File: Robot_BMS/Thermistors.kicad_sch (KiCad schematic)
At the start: 6 parts

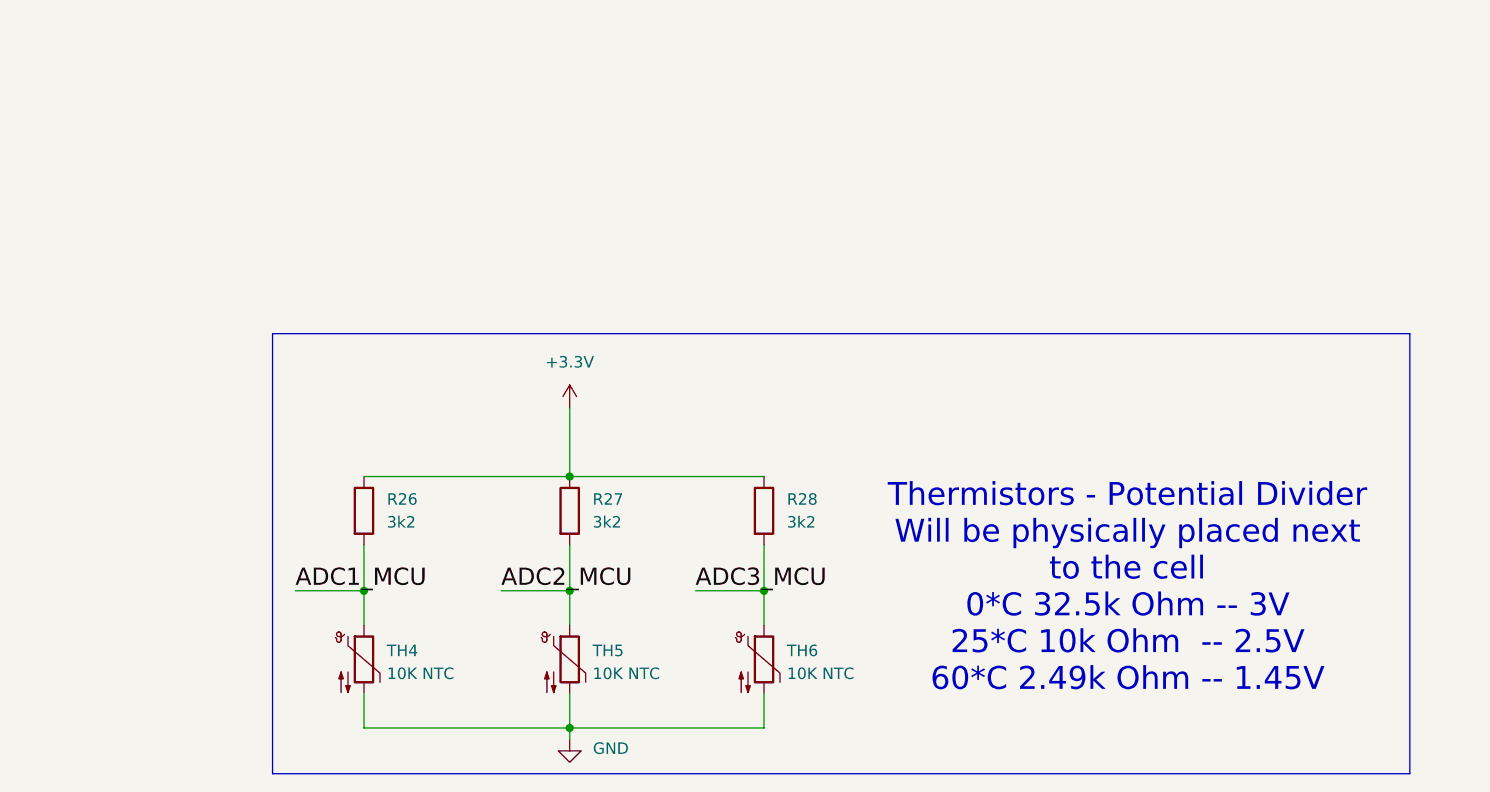
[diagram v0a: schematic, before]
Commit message: cleaning up hierarchical schematics
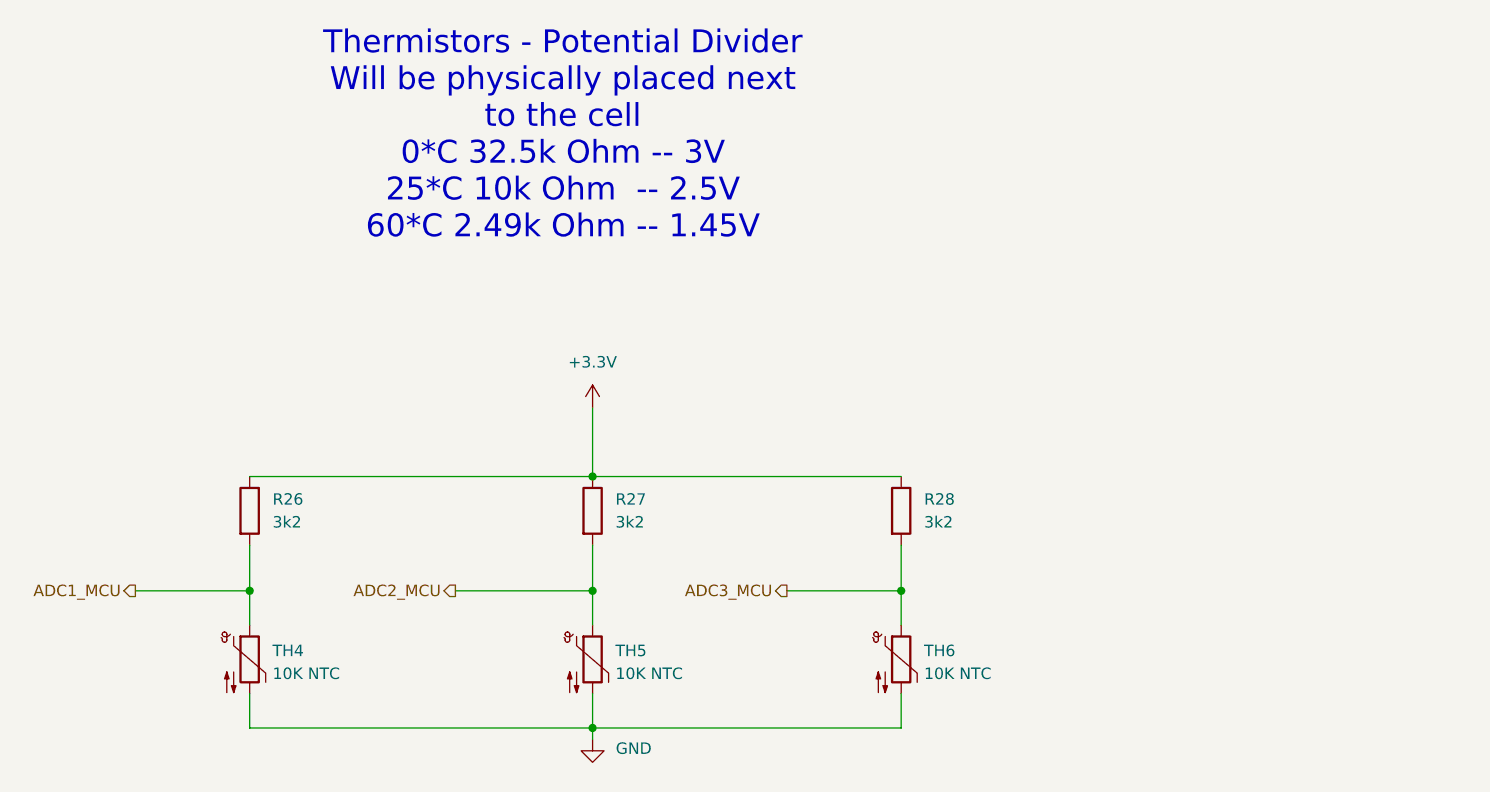
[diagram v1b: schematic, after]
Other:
- moved on the sheet: R26, R27, R28, TH4, TH5, TH6

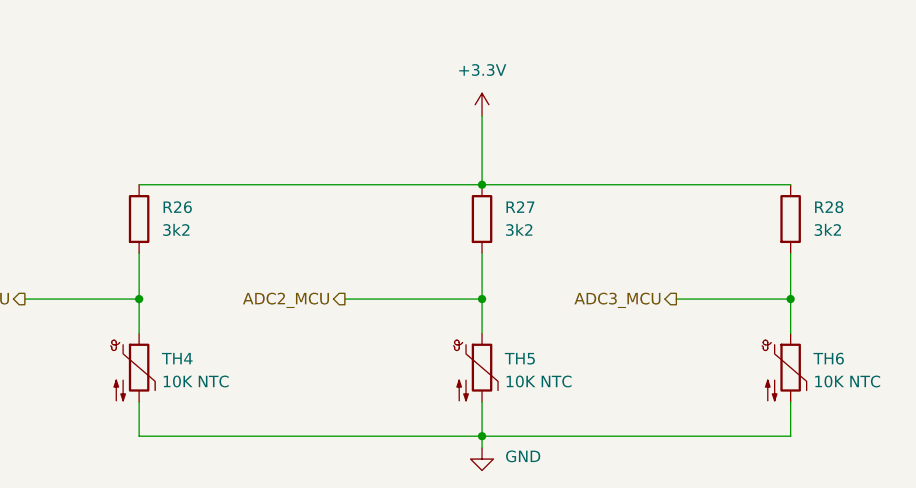
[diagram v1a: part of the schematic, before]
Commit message: DC power supply added via dc Barrel jack
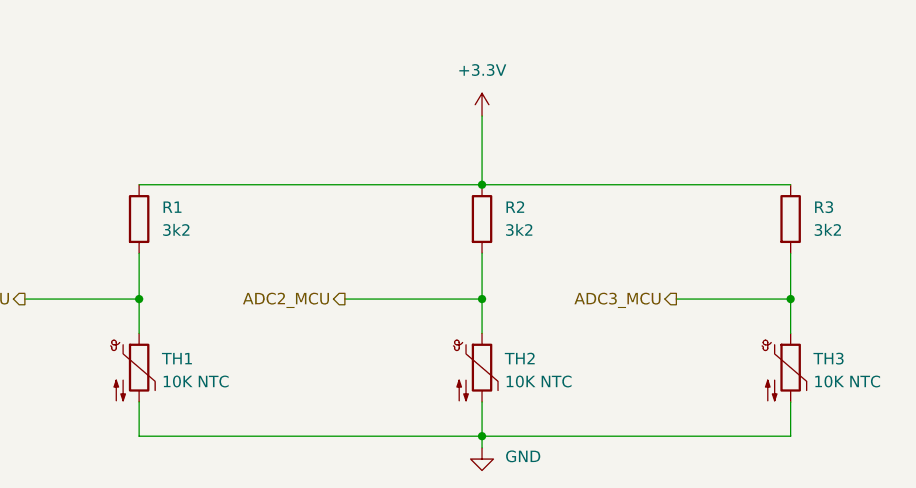
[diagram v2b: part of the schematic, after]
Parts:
- renumbered R26 to R1, R27 to R2, R28 to R3, TH4 to TH1, TH5 to TH2, TH6 to TH3
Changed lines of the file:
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@@
 		(dnp no)
 		(fields_autoplaced yes)
-		(property "Reference" "R26"
+		(property "Reference" "R1"
 			(at 96.52 101.5999 0)
 			(effects
@@
 			(project "Robot_BMS"
 				(path "/72551b1c-3d40-4199-8911-e5b015f4abec/cb04dfab-e035-4615-b482-7ed1936c63ff"
-					(reference "R26")
+					(reference "R1")
 					(unit 1)
 				)
@@
 		(dnp no)
 		(fields_autoplaced yes)
-		(property "Reference" "R28"
+		(property "Reference" "R3"
 			(at 168.91 101.5999 0)
 			(effects
@@
 			(project "Robot_BMS"
 				(path "/72551b1c-3d40-4199-8911-e5b015f4abec/cb04dfab-e035-4615-b482-7ed1936c63ff"
-					(reference "R28")
+					(reference "R3")
 					(unit 1)
 				)
@@
 		(dnp no)
 		(fields_autoplaced yes)
-		(property "Reference" "TH4"
+		(property "Reference" "TH1"
 			(at 96.52 118.4274 0)
 			(effects
@@
 			(project "Robot_BMS"
 				(path "/72551b1c-3d40-4199-8911-e5b015f4abec/cb04dfab-e035-4615-b482-7ed1936c63ff"
-					(reference "TH4")
+					(reference "TH1")
 					(unit 1)
 				)
@@
 		(dnp no)
 		(fields_autoplaced yes)
-		(property "Reference" "R27"
+		(property "Reference" "R2"
 			(at 134.62 101.5999 0)
 			(effects
@@
 			(project "Robot_BMS"
 				(path "/72551b1c-3d40-4199-8911-e5b015f4abec/cb04dfab-e035-4615-b482-7ed1936c63ff"
-					(reference "R27")
+					(reference "R2")
 					(unit 1)
 				)
@@
 		(on_board yes)
 		(dnp no)
-		(property "Reference" "#PWR010"
+		(property "Reference" "#PWR02"
 			(at 132.08 134.62 0)
 			(effects
@@
 			(project "Robot_BMS"
 				(path "/72551b1c-3d40-4199-8911-e5b015f4abec/cb04dfab-e035-4615-b482-7ed1936c63ff"
-					(reference "#PWR010")
+					(reference "#PWR02")
 					(unit 1)
 				)
@@
 		(dnp no)
 		(fields_autoplaced yes)
-		(property "Reference" "#PWR09"
+		(property "Reference" "#PWR01"
 			(at 132.08 95.25 0)
 			(effects
@@
 			(project "Robot_BMS"
 				(path "/72551b1c-3d40-4199-8911-e5b015f4abec/cb04dfab-e035-4615-b482-7ed1936c63ff"
-					(reference "#PWR09")
+					(reference "#PWR01")
 					(unit 1)
 				)
@@
 		(dnp no)
 		(fields_autoplaced yes)
-		(property "Reference" "TH6"
+		(property "Reference" "TH3"
 			(at 168.91 118.4274 0)
 			(effects
@@
 			(project "Robot_BMS"
 				(path "/72551b1c-3d40-4199-8911-e5b015f4abec/cb04dfab-e035-4615-b482-7ed1936c63ff"
-					(reference "TH6")
+					(reference "TH3")
 					(unit 1)
 				)
@@
 		(dnp no)
 		(fields_autoplaced yes)
-		(property "Reference" "TH5"
+		(property "Reference" "TH2"
 			(at 134.62 118.4274 0)
 			(effects
@@
 			(project "Robot_BMS"
 				(path "/72551b1c-3d40-4199-8911-e5b015f4abec/cb04dfab-e035-4615-b482-7ed1936c63ff"
-					(reference "TH5")
-					(unit 1)
-				)
+					(reference "TH2")
+					(unit 1)
+				)

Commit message: adding footprints and actual passive components
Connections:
- net +3.3V renamed 3V3
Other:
- note added: "All standard Passive componenets are 0603 imperial"
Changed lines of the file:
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@@
+	)
+	(junction
+		(at 137.414 91.44)
+		(diameter 0)
+		(color 0 0 0 0)
+	)
+	(junction
+		(at 132.08 91.44)
+		(diameter 0)
+		(color 0 0 0 0)
+	)
+	(junction
+		(at 132.08 128.27)
+		(diameter 0)
+		(color 0 0 0 0)
 	)
 	(junction
@@
 	(wire
 		(pts
+			(xy 137.414 91.44) (xy 139.192 91.44)
+		)
+		(stroke
+			(width 0)
+			(type default)
+		)
+	)
+	(wire
+		(pts
 			(xy 93.98 123.19) (xy 93.98 127)
 		)
@@
 		(pts
 			(xy 132.08 127) (xy 132.08 128.27)
+		)
+		(stroke
+			(width 0)
+			(type default)
+		)
+	)
+	(wire
+		(pts
+			(xy 132.08 91.44) (xy 137.414 91.44)
 		)
 		(stroke
@@
 				(size 2.54 2.54)
 			)
+		)
+	)
+	(text "All standard Passive\ncomponenets are 0603 imperial"
+		(exclude_from_sim no)
+		(at 213.868 175.768 0)
+		(effects
+			(font
+				(size 2.54 2.54)
+			)
+		)
+	)
+	(hierarchical_label "3V3"
+		(shape input)
+		(at 139.192 91.44 0)
+		(effects
+			(font
+				(size 1.27 1.27)
+			)
+			(justify left)
 		)
 	)
@@
 	)
 	(symbol
+		(lib_id "power:PWR_FLAG")
+		(at 137.414 91.44 180)
+		(unit 1)
+		(exclude_from_sim no)
+		(in_bom yes)
+		(on_board yes)
+		(dnp no)
+		(property "Reference" "#FLG02"
+			(at 137.414 93.345 0)
+			(effects
+				(font
+					(size 1.27 1.27)
+				)
+				(hide yes)
+			)
+		)
+		(property "Value" "PWR_FLAG"
+			(at 137.414 96.52 0)
+			(effects
+				(font
+					(size 1.27 1.27)
+				)
+			)
+		)
+		(property "Footprint" ""
+			(at 137.414 91.44 0)
+			(effects
+				(font
+					(size 1.27 1.27)
+				)
+				(hide yes)
+			)
+		)
+		(property "Datasheet" "~"
+			(at 137.414 91.44 0)
+			(effects
+				(font
+					(size 1.27 1.27)
+				)
+				(hide yes)
+			)
+		)
+		(property "Description" "Special symbol for telling ERC where power comes from"
+			(at 137.414 91.44 0)
+			(effects
+				(font
+					(size 1.27 1.27)
+				)
+				(hide yes)
+			)
+		)
+		(pin "1"
+		)
+		(instances
+			(project "Robot_BMS"
+				(path "/72551b1c-3d40-4199-8911-e5b015f4abec/cb04dfab-e035-4615-b482-7ed1936c63ff"
+					(reference "#FLG02")
+					(unit 1)
+				)
+			)
+		)
+	)
+	(symbol
 		(lib_id "Device:R")
 		(at 166.37 102.87 0)
@@
 	)
 	(symbol
+		(lib_id "power:PWR_FLAG")
+		(at 132.08 128.27 90)
+		(unit 1)
+		(exclude_from_sim no)
+		(in_bom yes)
+		(on_board yes)
+		(dnp no)
+		(property "Reference" "#FLG01"
+			(at 130.175 128.27 0)
+			(effects
+				(font
+					(size 1.27 1.27)
+				)
+				(hide yes)
+			)
+		)
+		(property "Value" "PWR_FLAG"
+			(at 123.444 128.524 90)
+			(effects
+				(font
+					(size 1.27 1.27)
+				)
+			)
+		)
+		(property "Footprint" ""
+			(at 132.08 128.27 0)
+			(effects
+				(font
+					(size 1.27 1.27)
+				)
+				(hide yes)
+			)
+		)
+		(property "Datasheet" "~"
+			(at 132.08 128.27 0)
+			(effects
+				(font
+					(size 1.27 1.27)
+				)
+				(hide yes)
+			)
+		)
+		(property "Description" "Special symbol for telling ERC where power comes from"
+			(at 132.08 128.27 0)
+			(effects
+				(font
+					(size 1.27 1.27)
+				)
+				(hide yes)
+			)
+		)
+		(pin "1"
+		)
+		(instances
+			(project "Robot_BMS"
+				(path "/72551b1c-3d40-4199-8911-e5b015f4abec/cb04dfab-e035-4615-b482-7ed1936c63ff"
+					(reference "#FLG01")
+					(unit 1)
+				)
+			)
+		)
+	)
+	(symbol
 		(lib_id "power:GND")
 		(at 132.08 128.27 0)
@@
 			)
 		)
-		(property "Value" "+3.3V"
+		(property "Value" "3V3"
 			(at 132.08 86.36 0)
 			(effects

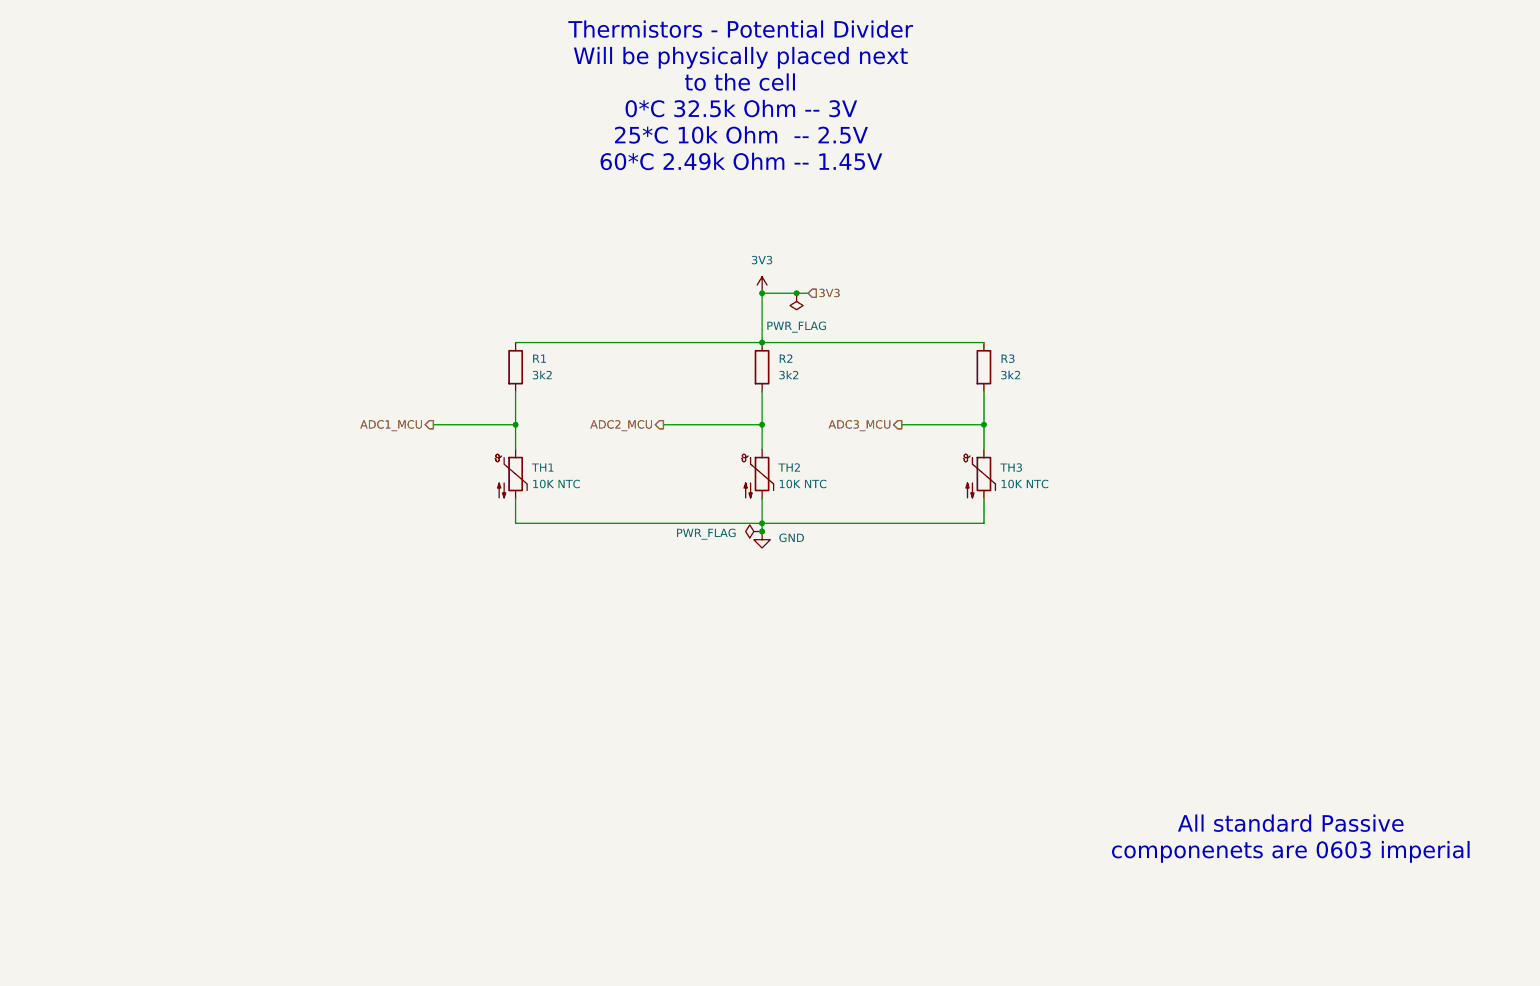
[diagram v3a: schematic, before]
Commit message: adding footprints and actual passive components pt.2
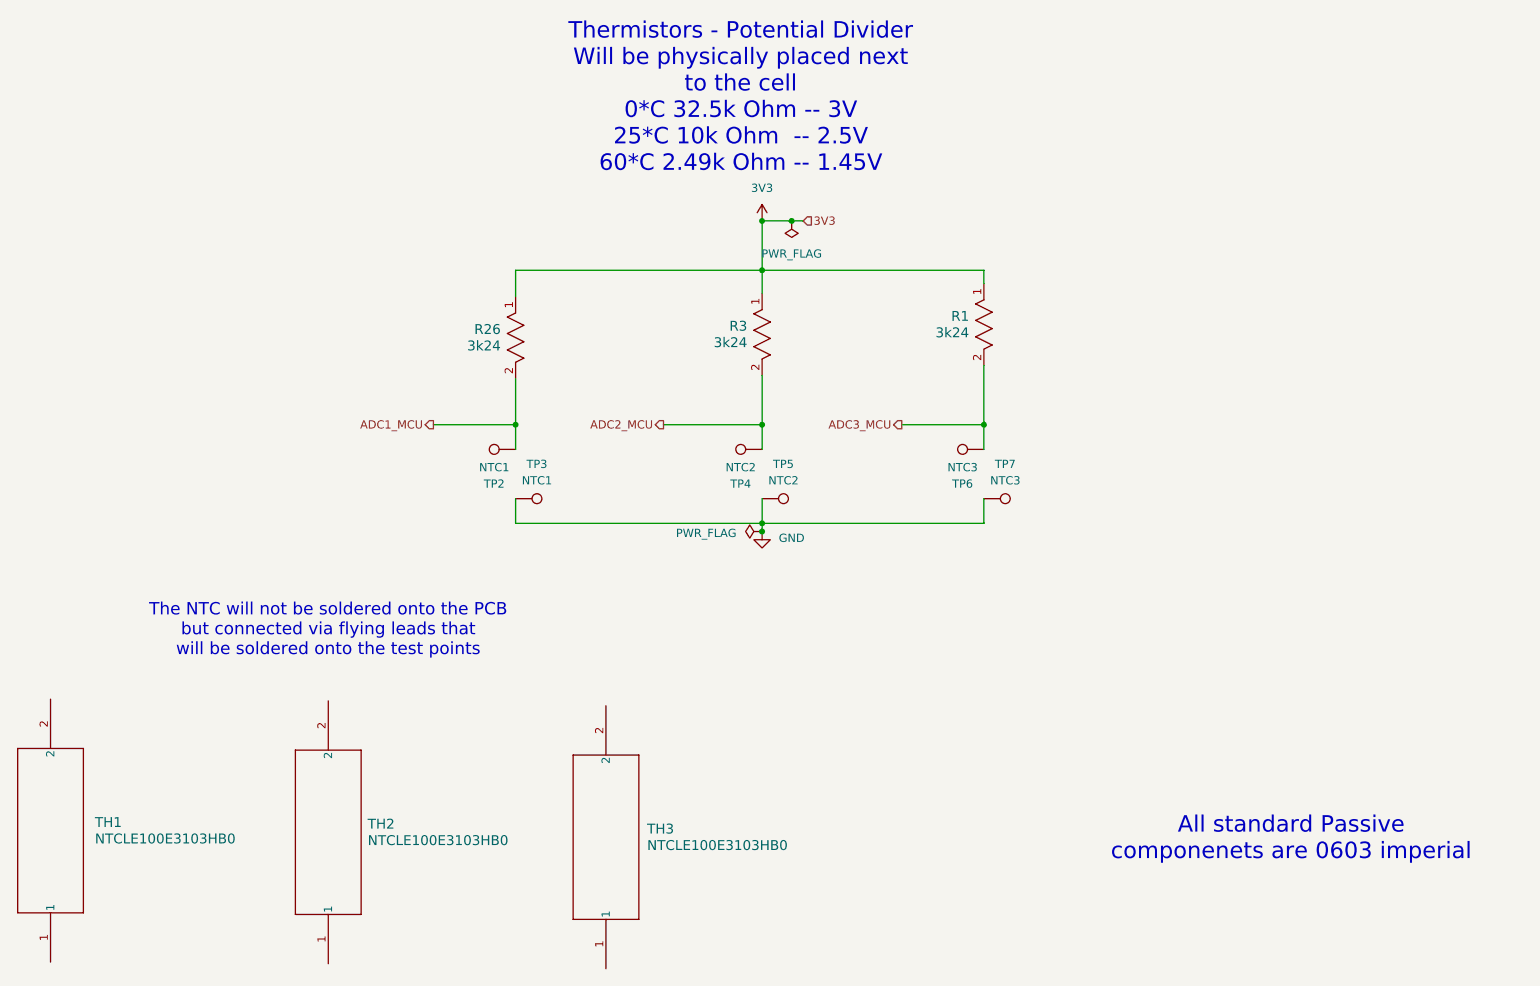
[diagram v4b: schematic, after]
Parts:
- removed R1, R2, R3: 3k2, symbol Device:R
- removed TH1, TH2, TH3: 10K NTC, symbol Device:Thermistor_NTC
- added R1, R26, R3: 3k24, RobotBMS:RC0603N_YAG, symbol RC0603FR_073K24L:RC0603FR-073K24L
- added TH1, TH2, TH3: NTCLE100E3103HB0, RobotBMS:THERMISTORS_100E3103HB0_VIS, symbol NTCLE100E3103HB0:NTCLE100E3103HB0
- added TP2, TP3: NTC1, TestPoint:TestPoint_Pad_D4.0mm, symbol Connector:TestPoint
- added TP4, TP5: NTC2, TestPoint:TestPoint_Pad_D4.0mm, symbol Connector:TestPoint
- added TP6, TP7: NTC3, TestPoint:TestPoint_Pad_D4.0mm, symbol Connector:TestPoint
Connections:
- net 3V3: now also R1.1, R26.1, R3.1
- net ADC1_MCU: now also R26.2, TP2.1
- net ADC2_MCU: now also R3.2, TP4.1
- net ADC3_MCU: now also R1.2, TP6.1
- net GND: now also TP3.1, TP5.1, TP7.1
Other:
- note added: "The NTC will not be soldered onto the PCB but connected via flying leads that will be soldered onto the test points"
